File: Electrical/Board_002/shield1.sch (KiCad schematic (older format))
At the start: 12 parts, among them P1 Power, P2 Analog, P3 Digital, P4 Digital, P5 CONN_01X01, P6 CONN_01X01, P7 CONN_01X01, P8 CONN_01X01

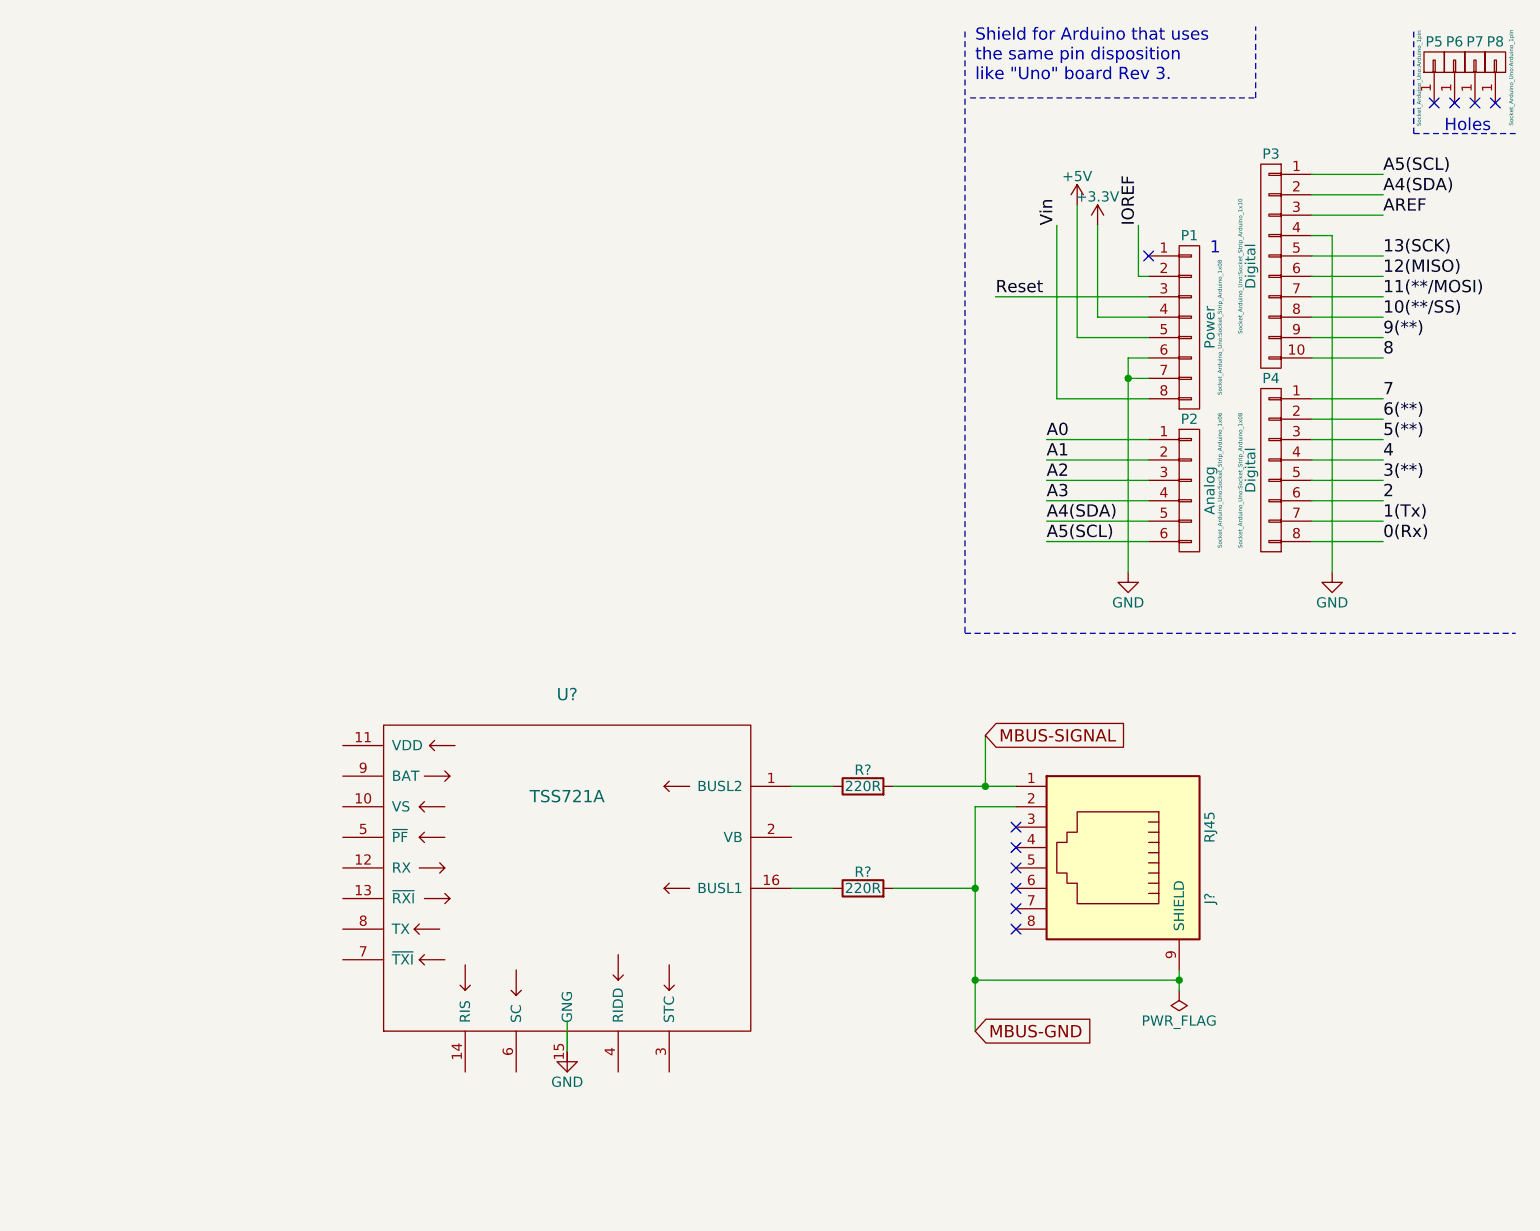
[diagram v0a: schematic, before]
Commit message: Board_002: Updated TSS721A component and put M-Bus electrical part into separate sheet
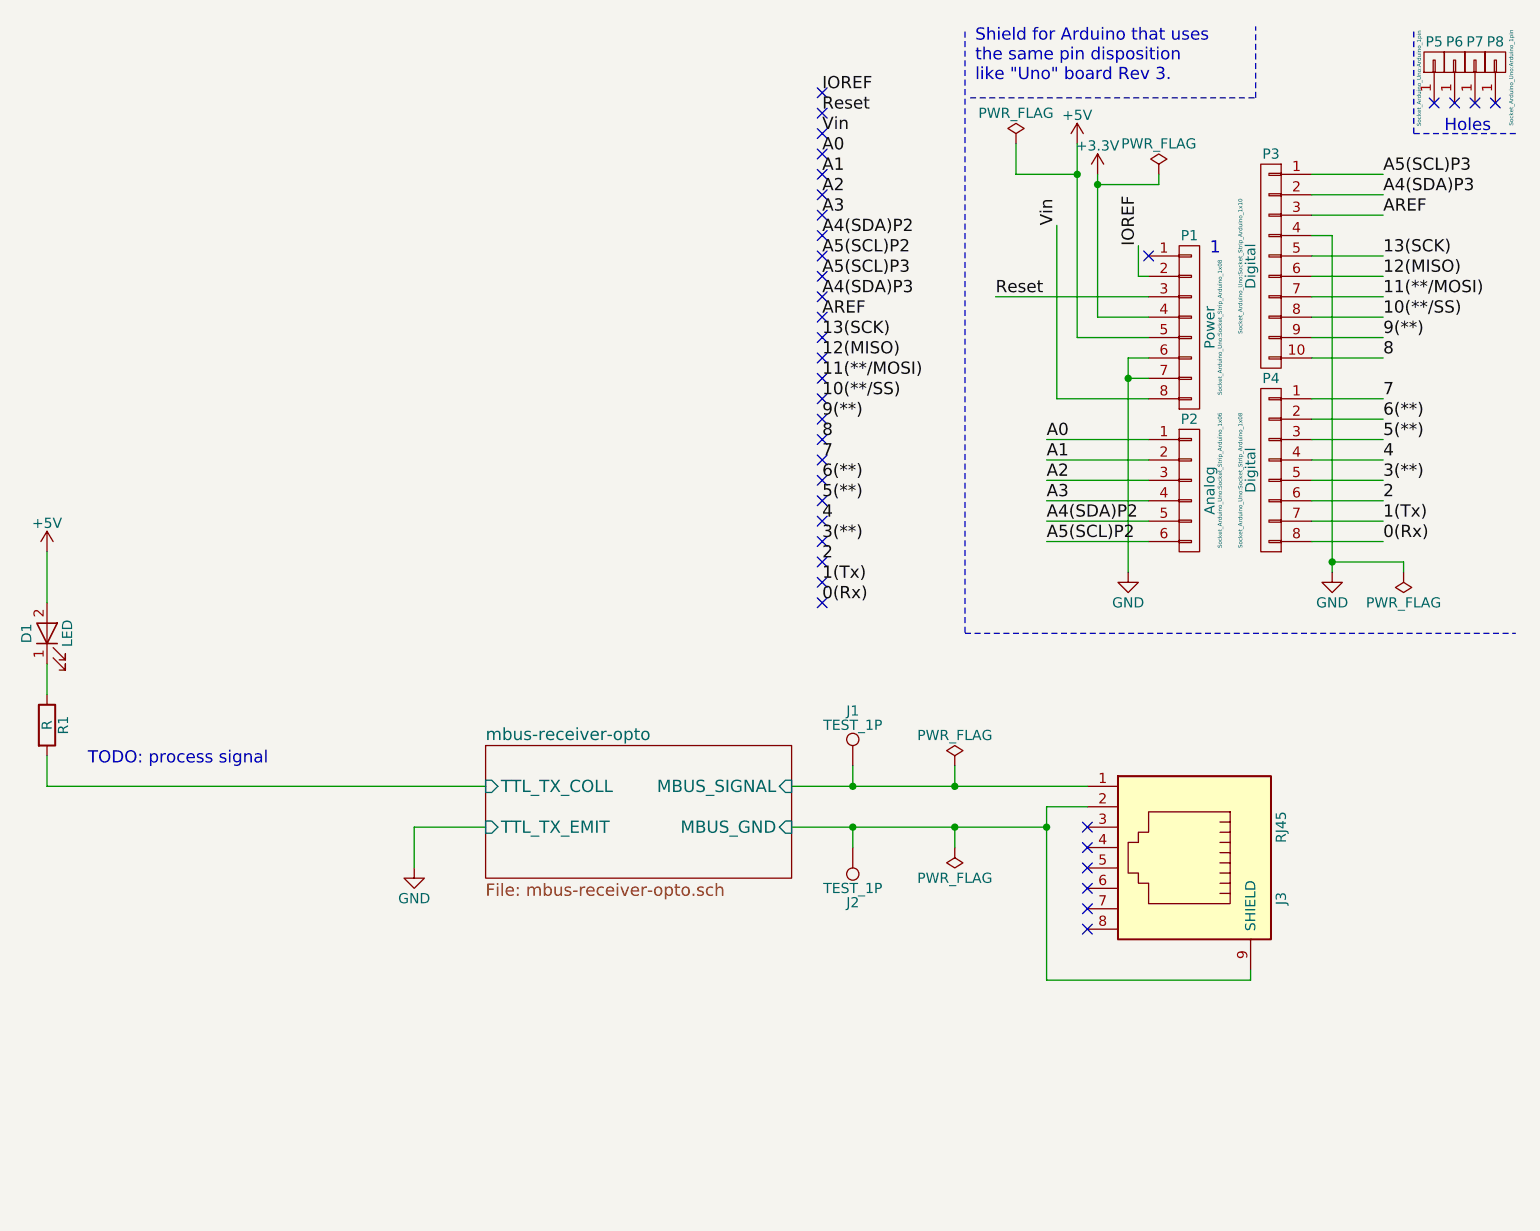
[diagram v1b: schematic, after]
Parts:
- removed R? (x2): 220R, symbol R
- removed U?: TSS721A, symbol TSS721A
- added D1: LED, symbol LED
- added J1, J2: TEST_1P, symbol TEST_1P
- added R1: R, symbol R
- gave numbers to parts that had none: 1
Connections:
- net +5V: now also D1.2 (A)
- net A4(SDA) renamed A4(SDA)P2
- net A4(SDA)P2: no longer P3.2 (P2)
- net A5(SCL) renamed A5(SCL)P2
- net A5(SCL)P2: no longer P3.1 (P1)
- net MBUS-GND renamed mbus-receiver-opto/MBUS_GND
- net mbus-receiver-opto/MBUS_GND: now also J2.1
- net MBUS-SIGNAL renamed mbus-receiver-opto/MBUS_SIGNAL
- net mbus-receiver-opto/MBUS_SIGNAL: now also J1.1
- new net: D1.1 (K), R1.1
- new net A4(SDA)P3: P3.2 (P2)
- new net A5(SCL)P3: P3.1 (P1)
- new net mbus-receiver-opto/TTL_TX_COLL: R1.2
- no-connect marks 11 -> 37
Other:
- note added: "TODO: process signal"
- moved on the sheet: J3

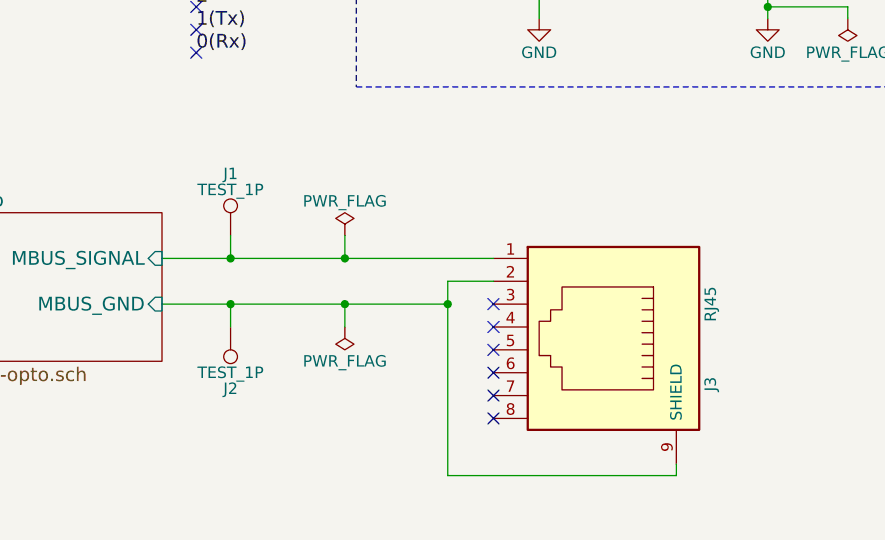
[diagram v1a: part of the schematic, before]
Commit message: Board_002: Add 2-pin connector to M-Bus
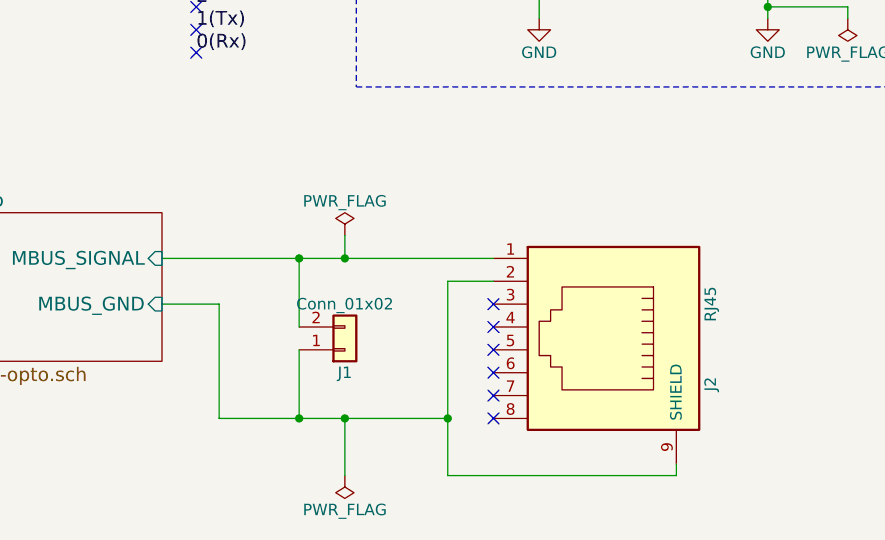
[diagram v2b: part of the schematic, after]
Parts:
- removed J1, J2: TEST_1P, symbol TEST_1P
- added J1: Conn_01x02, symbol Conn_01x02
- renumbered J3 to J2
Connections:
- net mbus-receiver-opto/MBUS_GND: now also J1.1 (Pin_1)
- net mbus-receiver-opto/MBUS_SIGNAL: now also J1.2 (Pin_2)
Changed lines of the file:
@@
 1
 $Comp
-L RJ45 J3
+L RJ45 J2
 U 1 1 5A5E7E25
 P 9550 4550
-F 0 "J3" H 9750 5050 50  0000 C CNN
+F 0 "J2" H 9750 5050 50  0000 C CNN
 F 1 "RJ45" H 9400 5050 50  0000 C CNN
 F 2 "" H 9550 4550 50  0001 C CNN
@@
 L PWR_FLAG #FLG05
 U 1 1 5A5E8423
-P 8450 4500
-F 0 "#FLG05" H 8450 4575 50  0001 C CNN
-F 1 "PWR_FLAG" H 8450 4650 50  0000 C CNN
-F 2 "" H 8450 4500 50  0001 C CNN
-F 3 "" H 8450 4500 50  0001 C CNN
-	1    8450 4500
+P 8450 5150
+F 0 "#FLG05" H 8450 5225 50  0001 C CNN
+F 1 "PWR_FLAG" H 8450 5300 50  0000 C CNN
+F 2 "" H 8450 5150 50  0001 C CNN
+F 3 "" H 8450 5150 50  0001 C CNN
+	1    8450 5150
 	-1   0    0    1
 $EndComp
@@
 	8900 5150 9900 5150
 Wire Wire Line
-	7650 4400 8900 4400
-Connection ~ 8900 4400
+	7900 4900 8900 4900
+Connection ~ 8900 4900
 Wire Wire Line
 	4000 3600 4000 3750
@@
 	9900 5150 9900 5100
 Wire Wire Line
-	8450 4500 8450 4400
-Connection ~ 8450 4400
-$Comp
-L TEST_1P J1
-U 1 1 5A62338F
-P 7950 4100
-F 0 "J1" H 7950 4370 50  0000 C CNN
-F 1 "TEST_1P" H 7950 4300 50  0000 C CNN
-F 2 "" H 8150 4100 50  0001 C CNN
-F 3 "" H 8150 4100 50  0001 C CNN
-	1    7950 4100
-	1    0    0    -1
-$EndComp
-Wire Wire Line
-	7950 4100 7950 4200
-Connection ~ 7950 4200
-$Comp
-L TEST_1P J2
-U 1 1 5A6234F0
-P 7950 4500
-F 0 "J2" H 7950 4770 50  0000 C CNN
-F 1 "TEST_1P" H 7950 4700 50  0000 C CNN
-F 2 "" H 8150 4500 50  0001 C CNN
-F 3 "" H 8150 4500 50  0001 C CNN
-	1    7950 4500
-	-1   0    0    1
-$EndComp
-Wire Wire Line
-	7950 4400 7950 4500
-Connection ~ 7950 4400
+	8450 5150 8450 4900
+Connection ~ 8450 4900
+$Comp
+L Conn_01x02 J1
+U 1 1 5A627909
+P 8450 4600
+F 0 "J1" H 8450 4700 50  0000 C CNN
+F 1 "Conn_01x02" H 8450 4400 50  0000 C CNN
+F 2 "" H 8450 4600 50  0001 C CNN
+F 3 "" H 8450 4600 50  0001 C CNN
+	1    8450 4600
+	1    0    0    1
+$EndComp
+Wire Wire Line
+	7650 4400 7900 4400
+Wire Wire Line
+	7900 4400 7900 4900
+Wire Wire Line
+	8250 4600 8250 4900
+Connection ~ 8250 4900
+Wire Wire Line
+	8250 4500 8250 4200
+Connection ~ 8250 4200
 $EndSCHEMATC
